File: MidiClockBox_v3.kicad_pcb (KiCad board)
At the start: 2 copper layers, 119.4 x 59.6 mm, 58 parts, among them J1 Midi In 0, J10 Display, J11 Midi Out 3, J12 Midi Out 4, J13 Midi Out 5, J14 Sync Out 0, J15 Sync Out 1, J2 ICSP, J3 Conn_02x09_Odd_Even, J4 Conn_02x04_Odd_Even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

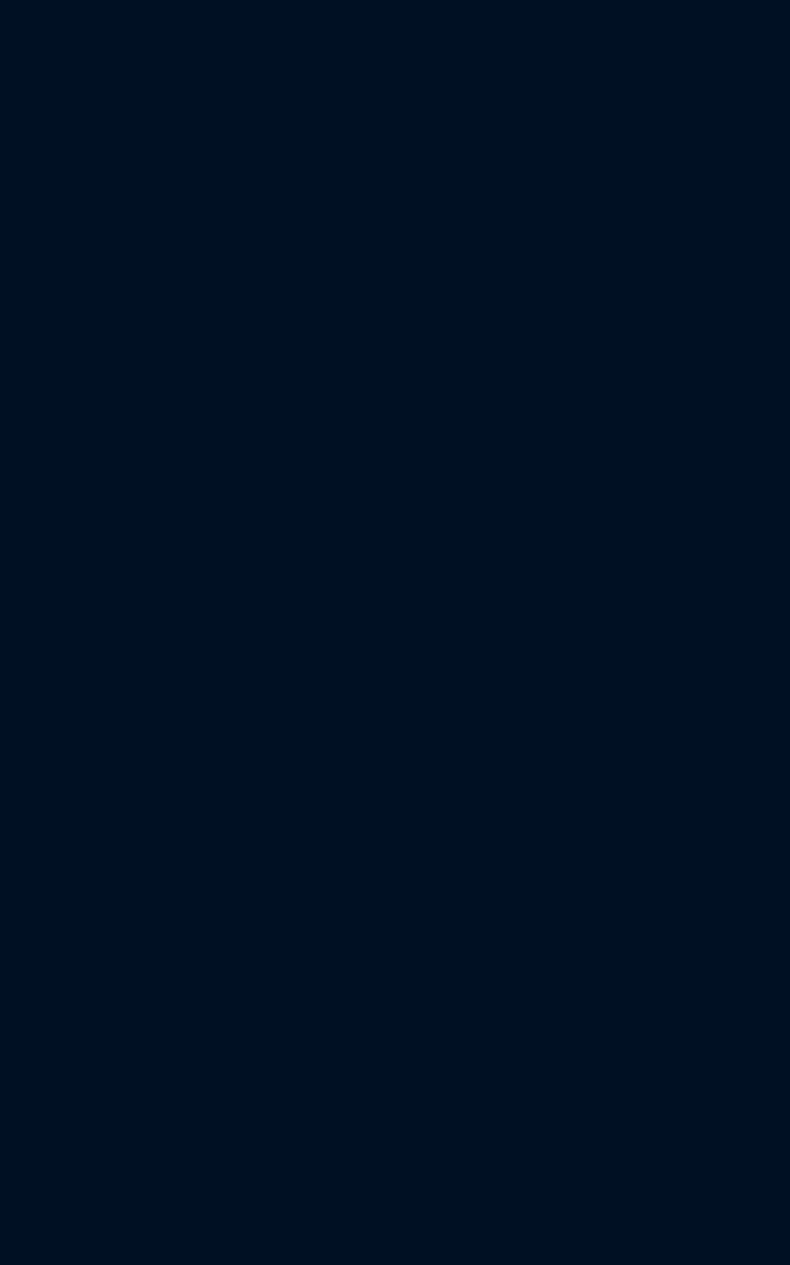
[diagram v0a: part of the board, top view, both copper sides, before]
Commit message: add parts to pcb
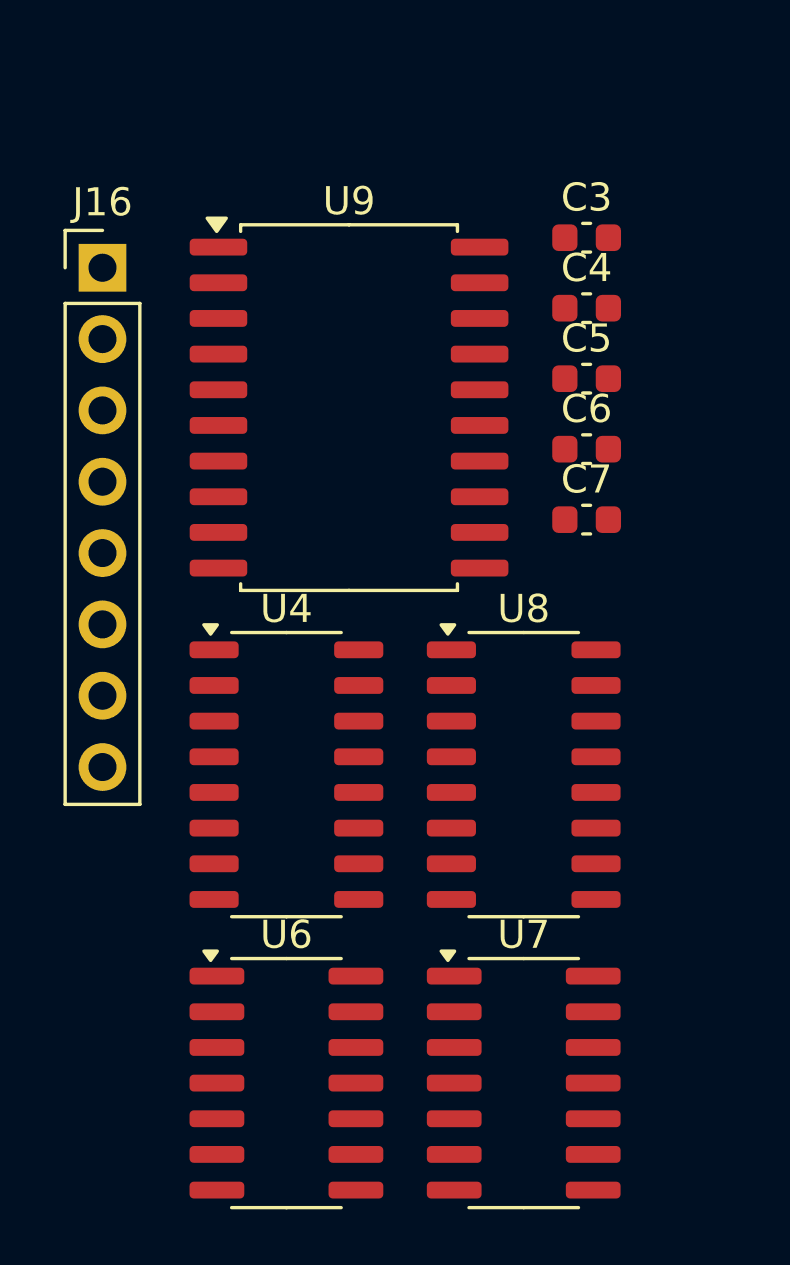
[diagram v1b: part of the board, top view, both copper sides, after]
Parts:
- added C3: 0.1µ, Capacitor_SMD:C_0603_1608Metric, F.Cu at (44.3, 125.6)
- added C4: 0.1µ, Capacitor_SMD:C_0603_1608Metric, F.Cu at (44.3, 128.1)
- added C5: 0.1µ, Capacitor_SMD:C_0603_1608Metric, F.Cu at (44.3, 130.6)
- added C6: 0.1µ, Capacitor_SMD:C_0603_1608Metric, F.Cu at (44.3, 133.1)
- added C7: 0.1µ, Capacitor_SMD:C_0603_1608Metric, F.Cu at (44.3, 135.6)
- added J16: Conn_01x08, Connector_PinHeader_2.54mm:PinHeader_1x08_P2.54mm_Vertical, F.Cu at (27.0, 126.7)
- added U4: 74HC595, Package_SO:SO-16_3.9x9.9mm_P1.27mm, F.Cu at (33.6, 144.7)
- added U6: 74LS08, Package_SO:SO-14_3.9x8.65mm_P1.27mm, F.Cu at (33.6, 155.7)
- added U7: 74LS08, Package_SO:SO-14_3.9x8.65mm_P1.27mm, F.Cu at (42.0, 155.7)
- added U8: 74HC595, Package_SO:SO-16_3.9x9.9mm_P1.27mm, F.Cu at (42.0, 144.7)
- added U9: 74LS241, Package_SO:SOIC-20W_7.5x12.8mm_P1.27mm, F.Cu at (35.8, 131.6)
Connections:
- net SYNC_OUT_0 renamed SYNC_TX_BUFFERED_0
- net SYNC_OUT_1 renamed SYNC_TX_BUFFERED_1
- J14 pad R: unconnected-(J14-PadR) -> SYNC_START_STOP_BUFFERED_0
- J15 pad R: unconnected-(J15-PadR) -> SYNC_START_STOP_BUFFERED_1
- J2 pad 4: MIDI_RX -> MOSI
- J5 pad 1: unconnected-(J5-Pin_1-Pad1) -> MIDI_TX
- J5 pad 14: MIDI_RX -> MOSI
- J5 pad 18: unconnected-(J5-Pin_18-Pad18) -> DA2
- J5 pad 2: unconnected-(J5-Pin_2-Pad2) -> MIDI_RX
- J5 pad 20: MIDI_TX -> SYNC_START_STOP
- J5 pad 7: unconnected-(J5-Pin_7-Pad7) -> DA0
- J5 pad 8: unconnected-(J5-Pin_8-Pad8) -> DA1
- U2 pad 11: MIDI_TX -> Net-(U2-I0b)
- U2 pad 13: MIDI_TX -> Net-(U2-I1b)
- U2 pad 15: SYNC_TX -> Net-(U2-I2b)
- U2 pad 17: SYNC_TX -> Net-(U2-I3b)
- U2 pad 2: MIDI_TX -> Net-(U2-I0a)
- U2 pad 4: MIDI_TX -> Net-(U2-I1a)
- U2 pad 6: MIDI_TX -> Net-(U2-I2a)
- U2 pad 8: MIDI_TX -> Net-(U2-I3a)

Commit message: add edge cuts
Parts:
- added C10: 0.1µ, Capacitor_SMD:C_0603_1608Metric, F.Cu at (88.0, 26.7)
- added C11: 0.1µ, Capacitor_SMD:C_0603_1608Metric, F.Cu at (103.0, 26.7)
- added C12: 0.1µ, Capacitor_SMD:C_0603_1608Metric, F.Cu at (128.5, 26.5)
- added C8: 0.1µ, Capacitor_SMD:C_0603_1608Metric, F.Cu at (58.0, 26.7)
- added C9: 0.1µ, Capacitor_SMD:C_0603_1608Metric, F.Cu at (73.0, 26.5)
- added D2: WS2812B, LED_SMD:LED_WS2812B_PLCC4_5.0x5.0mm_P3.2mm, F.Cu at (54.0, 27.5)
- added D3: WS2812B, LED_SMD:LED_WS2812B_PLCC4_5.0x5.0mm_P3.2mm, F.Cu at (69.0, 27.5)
- added D4: WS2812B, LED_SMD:LED_WS2812B_PLCC4_5.0x5.0mm_P3.2mm, F.Cu at (84.0, 27.5)
- added D5: WS2812B, LED_SMD:LED_WS2812B_PLCC4_5.0x5.0mm_P3.2mm, F.Cu at (99.0, 27.5)
- added D6: WS2812B, LED_SMD:LED_WS2812B_PLCC4_5.0x5.0mm_P3.2mm, F.Cu at (124.0, 27.5)
- added SW2: TAP, Button_Switch_THT:SW_PUSH-12mm_Wuerth-430476085716, F.Cu at (85.0, 60.8)
- added SW3: Start, Button_Switch_THT:SW_PUSH-12mm_Wuerth-430476085716, F.Cu at (60.0, 60.8)
- added SW4: Stop, Button_Switch_THT:SW_PUSH-12mm_Wuerth-430476085716, F.Cu at (110.0, 60.8)
- added SW5: Preset1, Button_Switch_THT:SW_PUSH-12mm_Wuerth-430476085716, F.Cu at (60.0, 80.8)
- added SW6: Preset2, Button_Switch_THT:SW_PUSH-12mm_Wuerth-430476085716, F.Cu at (85.0, 80.8)
- added SW7: Preset2, Button_Switch_THT:SW_PUSH-12mm_Wuerth-430476085716, F.Cu at (110.0, 80.8)
- added mouse-bite-2mm-slot: VAL**, Panelization:mouse-bite-2mm-slot, F.Cu at (143.0, 53.0)
- added mouse-bite-2mm-slot: VAL**, Panelization:mouse-bite-2mm-slot, F.Cu at (87.0, 36.0)
- added mouse-bite-2mm-slot: VAL**, Panelization:mouse-bite-2mm-slot, F.Cu at (131.0, 36.0)
- added mouse-bite-2mm-slot: VAL**, Panelization:mouse-bite-2mm-slot, F.Cu at (239.0, 70.0)
- added mouse-bite-2mm-slot: VAL**, Panelization:mouse-bite-2mm-slot, F.Cu at (65.0, 36.0)
- added mouse-bite-2mm-slot: VAL**, Panelization:mouse-bite-2mm-slot, F.Cu at (217.0, 70.0)
- added mouse-bite-2mm-slot: VAL**, Panelization:mouse-bite-2mm-slot, F.Cu at (143.0, 81.0)
- added mouse-bite-2mm-slot: VAL**, Panelization:mouse-bite-2mm-slot, F.Cu at (195.0, 70.0)
- added mouse-bite-2mm-slot: VAL**, Panelization:mouse-bite-2mm-slot, F.Cu at (143.0, 28.0)
- added mouse-bite-2mm-slot: VAL**, Panelization:mouse-bite-2mm-slot, F.Cu at (43.0, 36.0)
- added mouse-bite-2mm-slot: VAL**, Panelization:mouse-bite-2mm-slot, F.Cu at (109.0, 36.0)
- added mouse-bite-2mm-slot: VAL**, Panelization:mouse-bite-2mm-slot, F.Cu at (151.0, 70.0)
- added mouse-bite-2mm-slot: VAL**, Panelization:mouse-bite-2mm-slot, F.Cu at (173.0, 70.0)
- J16: value Conn_01x08 -> Spare
- J3: value Conn_02x09_Odd_Even -> WS2812; footprint Connector_PinHeader_2.54mm:PinHeader_2x09_P2.54mm_Vertical -> Connector_PinHeader_2.54mm:PinHeader_1x03_P2.54mm_Vertical
- J4: value Conn_02x04_Odd_Even -> Conn_02x07_Odd_Even; footprint Connector_PinHeader_2.54mm:PinHeader_2x04_P2.54mm_Vertical -> Connector_PinHeader_2.54mm:PinHeader_2x07_P2.54mm_Vertical
- moved U9 201.8 mm to (221.1, 51.7), turned to 180 degrees
- moved J16 197.8 mm to (215.0, 65.0), turned to 90 degrees
- moved U7 194.5 mm to (207.6, 53.7)
- moved U6 193.8 mm to (197.1, 51.7)
- moved C7 189.1 mm to (217.6, 59.9), turned to 180 degrees
- moved C5 185.9 mm to (210.6, 47.7)
- moved C6 178.5 mm to (200.1, 46.0)
- moved U4 178.1 mm to (186.6, 53.7)
- moved C3 164.7 mm to (189.2, 47.2)
- moved U8 162.5 mm to (176.6, 53.7)
- moved C4 157.5 mm to (179.3, 47.0)
- moved U2 121.7 mm to (237.6, 53.2), turned to 0 degrees
- moved C1 119.7 mm to (240.9, 45.5), turned to 180 degrees
- moved J11 116.6 mm to (204.2, 28.5)
- moved J13 116.6 mm to (192.8, 28.5)
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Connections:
- net IN_12 renamed ENC_SW
- net IN_13 renamed ENC_A
- net IN_14 renamed ENC_B
- J3 pad 1: IN_0 -> GND
- J3 pad 2: +5V -> Net-(D2-DIN)
- J3 pad 3: IN_1 -> +5V
- J4 pad 1: IN_9 -> IN_6
- J4 pad 3: IN_10 -> IN_7
- J4 pad 5: IN_11 -> IN_8
- J4 pad 7: IN_15 -> IN_9
- R12 pad 1: IN_5 -> IN_PRESET3
- R13 pad 1: IN_4 -> IN_PRESET2
- R14 pad 1: IN_3 -> IN_PRESET1
- R15 pad 1: IN_2 -> IN_STOP
- R16 pad 1: IN_1 -> IN_START
- R17 pad 1: IN_0 -> IN_TAP
- U1 pad 4: IN_5 -> IN_PRESET3
- U1 pad 5: IN_4 -> IN_PRESET2
- U1 pad 6: IN_3 -> IN_PRESET1
- U1 pad 7: IN_2 -> IN_STOP
- U1 pad 8: IN_1 -> IN_START
- U1 pad 9: IN_0 -> IN_TAP
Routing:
- net +5V: track 401.8 -> 0.00 mm
- net GND: track 116.9 -> 0.00 mm, vias 28 -> 0
- net MIDI_RX: track 104.9 -> 0.00 mm
- net MIDI_TX: track 89.1 -> 0.00 mm, vias 4 -> 0
- net ENC_A: track 54.8 -> 0.00 mm
- net MIDI_OUT_4: track 51.8 -> 0.00 mm
- net ENC_B: track 50.7 -> 0.00 mm
- net SYNC_TX: track 47.9 -> 0.00 mm, vias 2 -> 0
- net SDA: track 44.2 -> 0.00 mm
- net SCL: track 44.1 -> 0.00 mm
- net MIDI_OUT_5: track 43.3 -> 0.00 mm
- net DEMUX: track 42.8 -> 0.00 mm, vias 2 -> 0
- net MIDI_OUT_3: track 42.5 -> 0.00 mm
- net MISO: track 38.5 -> 0.00 mm
- net LED_DATA: track 37.5 -> 0.00 mm
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- removed copper zone on B.Cu, net GND
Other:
- board size 119.4 x 59.6 mm -> 219 x 70 mm
- board text added: "Extra button?"
- board text added: "Ports auf single board incl Arduino LED Stripe einzeln Buttons auf single board, wenig zuleitung, 2-seitig Panelize"
- board text removed: "FSW1"
- board text removed: "FSW2"
- board text removed: "FSW3"
- board text removed: "GND"
- board text removed: "In 15 11 10 9"
- board text removed: "Pre1"
- board text removed: "Pre2"
- board text removed: "Pre3"
- board text removed: "SCL"
- board text removed: "SDA"
- board text removed: "Start"
- board text removed: "Stop"
- board text removed: "Tap"
- board text removed: "Vcc"

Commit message: change layout
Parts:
- removed mouse-bite-2mm-slot (x13): VAL**, Panelization:mouse-bite-2mm-slot
- moved C1 127.6 mm to (114.7, 63.9), turned to -90 degrees
- moved C2 111.2 mm to (234.2, 45.0), turned to 0 degrees
- moved SW3 55.0 mm to (107.0, 89.5), turned to 90 degrees
- moved SW2 40.8 mm to (125.0, 52.5), turned to 90 degrees
- moved R4 33.7 mm to (97.0, 72.7)
- moved SW7 33.3 mm to (78.0, 90.0), turned to 90 degrees
- moved SW4 32.6 mm to (124.5, 90.0), turned to 90 degrees
- moved J4 31.6 mm to (89.0, 101.3)
- moved D1 30.2 mm to (186.5, 80.0), turned to 90 degrees
- moved R10 26.4 mm to (187.0, 84.5), turned to -90 degrees
- moved SW6 24.8 mm to (62.0, 90.0), turned to 90 degrees
- moved R18 21.0 mm to (217.0, 79.3)
- moved R19 21.0 mm to (217.0, 81.8)
- moved R20 21.0 mm to (217.0, 76.7)
- moved U3 21.0 mm to (209.0, 80.5)
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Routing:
- net S3: vias 0 -> 1
- net (no net): vias 18 -> 15
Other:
- outline, holes or cut-outs redrawn
- board text removed: "Extra button?"

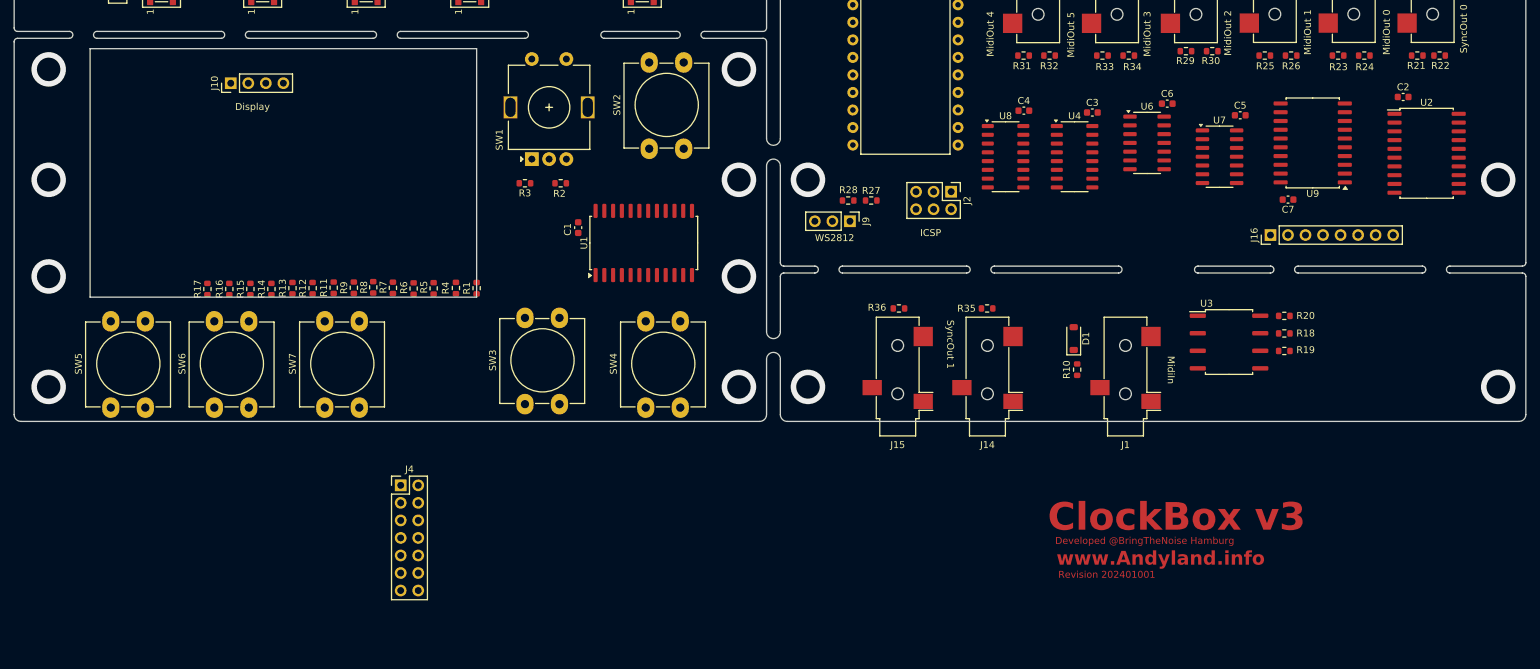
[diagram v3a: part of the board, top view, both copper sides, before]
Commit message: increase size to something useful
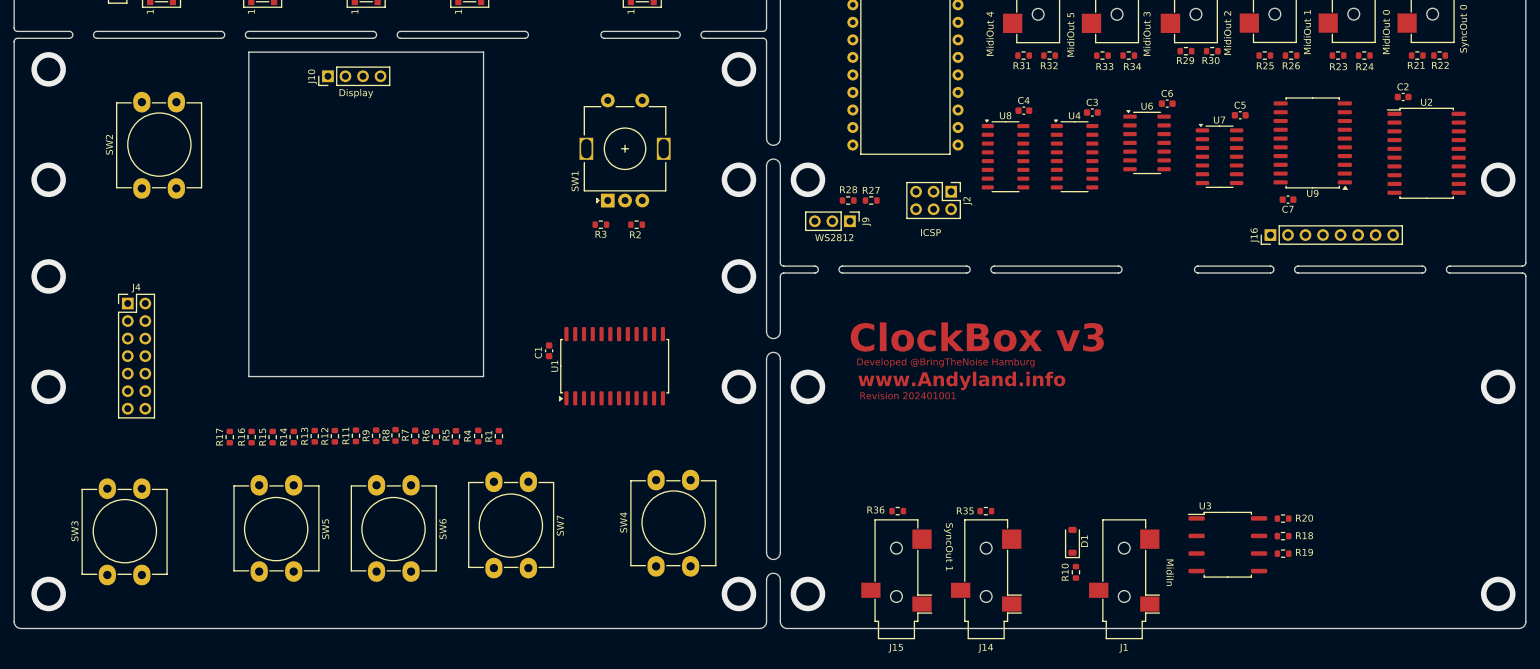
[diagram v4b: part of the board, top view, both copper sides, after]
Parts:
- SW7: value Preset2 -> Preset3
- moved SW2 73.7 mm to (51.5, 58.2)
- moved SW3 65.4 mm to (46.5, 114.2)
- moved J4 47.5 mm to (49.5, 74.9)
- moved SW7 31.4 mm to (107.5, 100.8), turned to -90 degrees
- moved SW6 30.6 mm to (90.5, 101.2), turned to -90 degrees
- moved D1 29.4 mm to (186.3, 109.4)
- moved J1 29.4 mm to (193.8, 114.9)
- moved J14 29.4 mm to (173.8, 114.9)
- moved J15 29.4 mm to (160.8, 114.9)
- moved R10 29.4 mm to (186.8, 113.9)
- moved R18 29.4 mm to (216.8, 108.6)
- moved R19 29.4 mm to (216.8, 111.2)
- moved R20 29.4 mm to (216.8, 106.1)
- moved R35 29.4 mm to (173.8, 105.0)
- moved R36 29.4 mm to (161.0, 105.0)
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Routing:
- net (no net): vias 15 -> 19
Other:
- board size 219 x 70 mm -> 219 x 100 mm
